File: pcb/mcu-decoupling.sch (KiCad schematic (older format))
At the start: 21 parts

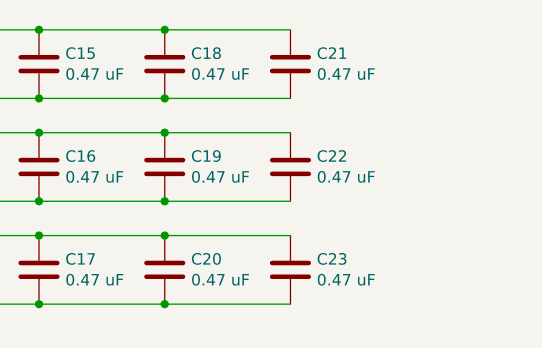
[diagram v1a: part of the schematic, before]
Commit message: Finished schematic signoff review. Fixed oscillator pinout bug, added some test points.
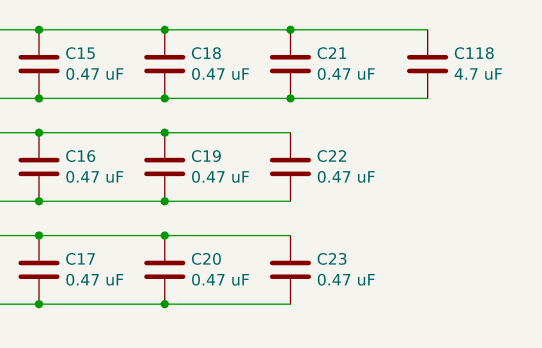
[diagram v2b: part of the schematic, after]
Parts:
- added C118: 4.7 uF, symbol device:C
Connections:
- net 3V3: now also C118.1
- net GND: now also C118.2
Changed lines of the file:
@@
 Sheet 3 8
 Title "INTEGRALSTICK Compute Module"
-Date "2018-11-07"
+Date "2018-11-09"
 Rev "0.1"
 Comp "Andrew D. Zonenberg"
@@
 Wire Wire Line
 	4750 4500 4200 4500
+$Comp
+L device:C C118
+U 1 1 5D2E7FF4
+P 7550 3300
+F 0 "C118" H 7665 3346 50  0000 L CNN
+F 1 "4.7 uF" H 7665 3255 50  0000 L CNN
+F 2 "" H 7588 3150 50  0001 C CNN
+F 3 "" H 7550 3300 50  0001 C CNN
+	1    7550 3300
+	1    0    0    -1
+$EndComp
+Wire Wire Line
+	7550 3450 6950 3450
+Connection ~ 6950 3450
+Wire Wire Line
+	7550 3150 6950 3150
+Connection ~ 6950 3150
 $EndSCHEMATC

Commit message: Assigned lots of footprints. Still have a few to go.
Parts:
- C10, C11, C12, C13, C14, C15, C16, C17, C18, C19, C20, C21, C22, C23, C4, C5, C6, C7, C8, C9: footprint (none) -> azonenberg_pcb:EIA_0402_CAP_NOSILK
- C118, C3: footprint (none) -> azonenberg_pcb:EIA_0603_CAP_NOSILK
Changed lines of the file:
@@
 F 0 "C3" H 3765 3346 50  0000 L CNN
 F 1 "4.7 uF" H 3765 3255 50  0000 L CNN
-F 2 "" H 3688 3150 50  0001 C CNN
+F 2 "azonenberg_pcb:EIA_0603_CAP_NOSILK" H 3688 3150 50  0001 C CNN
 F 3 "" H 3650 3300 50  0001 C CNN
 	1    3650 3300
@@
 F 0 "C4" H 4315 3346 50  0000 L CNN
 F 1 "0.47 uF" H 4315 3255 50  0000 L CNN
-F 2 "" H 4238 3150 50  0001 C CNN
+F 2 "azonenberg_pcb:EIA_0402_CAP_NOSILK" H 4238 3150 50  0001 C CNN
 F 3 "" H 4200 3300 50  0001 C CNN
 	1    4200 3300
@@
 F 0 "C8" H 4865 3346 50  0000 L CNN
 F 1 "0.47 uF" H 4865 3255 50  0000 L CNN
-F 2 "" H 4788 3150 50  0001 C CNN
+F 2 "azonenberg_pcb:EIA_0402_CAP_NOSILK" H 4788 3150 50  0001 C CNN
 F 3 "" H 4750 3300 50  0001 C CNN
 	1    4750 3300
@@
 F 0 "C12" H 5415 3346 50  0000 L CNN
 F 1 "0.47 uF" H 5415 3255 50  0000 L CNN
-F 2 "" H 5338 3150 50  0001 C CNN
+F 2 "azonenberg_pcb:EIA_0402_CAP_NOSILK" H 5338 3150 50  0001 C CNN
 F 3 "" H 5300 3300 50  0001 C CNN
 	1    5300 3300
@@
 F 0 "C15" H 5965 3346 50  0000 L CNN
 F 1 "0.47 uF" H 5965 3255 50  0000 L CNN
-F 2 "" H 5888 3150 50  0001 C CNN
+F 2 "azonenberg_pcb:EIA_0402_CAP_NOSILK" H 5888 3150 50  0001 C CNN
 F 3 "" H 5850 3300 50  0001 C CNN
 	1    5850 3300
@@
 F 0 "C18" H 6515 3346 50  0000 L CNN
 F 1 "0.47 uF" H 6515 3255 50  0000 L CNN
-F 2 "" H 6438 3150 50  0001 C CNN
+F 2 "azonenberg_pcb:EIA_0402_CAP_NOSILK" H 6438 3150 50  0001 C CNN
 F 3 "" H 6400 3300 50  0001 C CNN
 	1    6400 3300
@@
 F 0 "C21" H 7065 3346 50  0000 L CNN
 F 1 "0.47 uF" H 7065 3255 50  0000 L CNN
-F 2 "" H 6988 3150 50  0001 C CNN
+F 2 "azonenberg_pcb:EIA_0402_CAP_NOSILK" H 6988 3150 50  0001 C CNN
 F 3 "" H 6950 3300 50  0001 C CNN
 	1    6950 3300
@@
 F 0 "C5" H 4315 3796 50  0000 L CNN
 F 1 "0.47 uF" H 4315 3705 50  0000 L CNN
-F 2 "" H 4238 3600 50  0001 C CNN
+F 2 "azonenberg_pcb:EIA_0402_CAP_NOSILK" H 4238 3600 50  0001 C CNN
 F 3 "" H 4200 3750 50  0001 C CNN
 	1    4200 3750
@@
 F 0 "C9" H 4865 3796 50  0000 L CNN
 F 1 "0.47 uF" H 4865 3705 50  0000 L CNN
-F 2 "" H 4788 3600 50  0001 C CNN
+F 2 "azonenberg_pcb:EIA_0402_CAP_NOSILK" H 4788 3600 50  0001 C CNN
 F 3 "" H 4750 3750 50  0001 C CNN
 	1    4750 3750
@@
 F 0 "C13" H 5415 3796 50  0000 L CNN
 F 1 "0.47 uF" H 5415 3705 50  0000 L CNN
-F 2 "" H 5338 3600 50  0001 C CNN
+F 2 "azonenberg_pcb:EIA_0402_CAP_NOSILK" H 5338 3600 50  0001 C CNN
 F 3 "" H 5300 3750 50  0001 C CNN
 	1    5300 3750
@@
 F 0 "C16" H 5965 3796 50  0000 L CNN
 F 1 "0.47 uF" H 5965 3705 50  0000 L CNN
-F 2 "" H 5888 3600 50  0001 C CNN
+F 2 "azonenberg_pcb:EIA_0402_CAP_NOSILK" H 5888 3600 50  0001 C CNN
 F 3 "" H 5850 3750 50  0001 C CNN
 	1    5850 3750
@@
 F 0 "C19" H 6515 3796 50  0000 L CNN
 F 1 "0.47 uF" H 6515 3705 50  0000 L CNN
-F 2 "" H 6438 3600 50  0001 C CNN
+F 2 "azonenberg_pcb:EIA_0402_CAP_NOSILK" H 6438 3600 50  0001 C CNN
 F 3 "" H 6400 3750 50  0001 C CNN
 	1    6400 3750
@@
 F 0 "C22" H 7065 3796 50  0000 L CNN
 F 1 "0.47 uF" H 7065 3705 50  0000 L CNN
-F 2 "" H 6988 3600 50  0001 C CNN
+F 2 "azonenberg_pcb:EIA_0402_CAP_NOSILK" H 6988 3600 50  0001 C CNN
 F 3 "" H 6950 3750 50  0001 C CNN
 	1    6950 3750
@@
 F 0 "C6" H 4315 4246 50  0000 L CNN
 F 1 "0.47 uF" H 4315 4155 50  0000 L CNN
-F 2 "" H 4238 4050 50  0001 C CNN
+F 2 "azonenberg_pcb:EIA_0402_CAP_NOSILK" H 4238 4050 50  0001 C CNN
 F 3 "" H 4200 4200 50  0001 C CNN
 	1    4200 4200
@@
 F 0 "C10" H 4865 4246 50  0000 L CNN
 F 1 "0.47 uF" H 4865 4155 50  0000 L CNN
-F 2 "" H 4788 4050 50  0001 C CNN
+F 2 "azonenberg_pcb:EIA_0402_CAP_NOSILK" H 4788 4050 50  0001 C CNN
 F 3 "" H 4750 4200 50  0001 C CNN
 	1    4750 4200
@@
 F 0 "C14" H 5415 4246 50  0000 L CNN
 F 1 "0.47 uF" H 5415 4155 50  0000 L CNN
-F 2 "" H 5338 4050 50  0001 C CNN
+F 2 "azonenberg_pcb:EIA_0402_CAP_NOSILK" H 5338 4050 50  0001 C CNN
 F 3 "" H 5300 4200 50  0001 C CNN
 	1    5300 4200
@@
 F 0 "C17" H 5965 4246 50  0000 L CNN
 F 1 "0.47 uF" H 5965 4155 50  0000 L CNN
-F 2 "" H 5888 4050 50  0001 C CNN
+F 2 "azonenberg_pcb:EIA_0402_CAP_NOSILK" H 5888 4050 50  0001 C CNN
 F 3 "" H 5850 4200 50  0001 C CNN
 	1    5850 4200
@@
 F 0 "C20" H 6515 4246 50  0000 L CNN
 F 1 "0.47 uF" H 6515 4155 50  0000 L CNN
-F 2 "" H 6438 4050 50  0001 C CNN
+F 2 "azonenberg_pcb:EIA_0402_CAP_NOSILK" H 6438 4050 50  0001 C CNN
 F 3 "" H 6400 4200 50  0001 C CNN
 	1    6400 4200
@@
 F 0 "C23" H 7065 4246 50  0000 L CNN
 F 1 "0.47 uF" H 7065 4155 50  0000 L CNN
-F 2 "" H 6988 4050 50  0001 C CNN
+F 2 "azonenberg_pcb:EIA_0402_CAP_NOSILK" H 6988 4050 50  0001 C CNN
 F 3 "" H 6950 4200 50  0001 C CNN
 	1    6950 4200
@@
 F 0 "C7" H 4315 4696 50  0000 L CNN
 F 1 "0.47 uF" H 4315 4605 50  0000 L CNN
-F 2 "" H 4238 4500 50  0001 C CNN
+F 2 "azonenberg_pcb:EIA_0402_CAP_NOSILK" H 4238 4500 50  0001 C CNN
 F 3 "" H 4200 4650 50  0001 C CNN
 	1    4200 4650
@@
 F 0 "C11" H 4865 4696 50  0000 L CNN
 F 1 "0.47 uF" H 4865 4605 50  0000 L CNN
-F 2 "" H 4788 4500 50  0001 C CNN
+F 2 "azonenberg_pcb:EIA_0402_CAP_NOSILK" H 4788 4500 50  0001 C CNN
 F 3 "" H 4750 4650 50  0001 C CNN
 	1    4750 4650
@@
 F 0 "C118" H 7665 3346 50  0000 L CNN
 F 1 "4.7 uF" H 7665 3255 50  0000 L CNN
-F 2 "" H 7588 3150 50  0001 C CNN
+F 2 "azonenberg_pcb:EIA_0603_CAP_NOSILK" H 7588 3150 50  0001 C CNN
 F 3 "" H 7550 3300 50  0001 C CNN
 	1    7550 3300
